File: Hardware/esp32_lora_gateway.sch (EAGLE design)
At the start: 36 parts, among them J5 U.FL, Q2 MBT3904DW1T1, U1 ESP-WROOM-32NARROW, U2 RFM96W, U3 3.3V, U5 CH340C

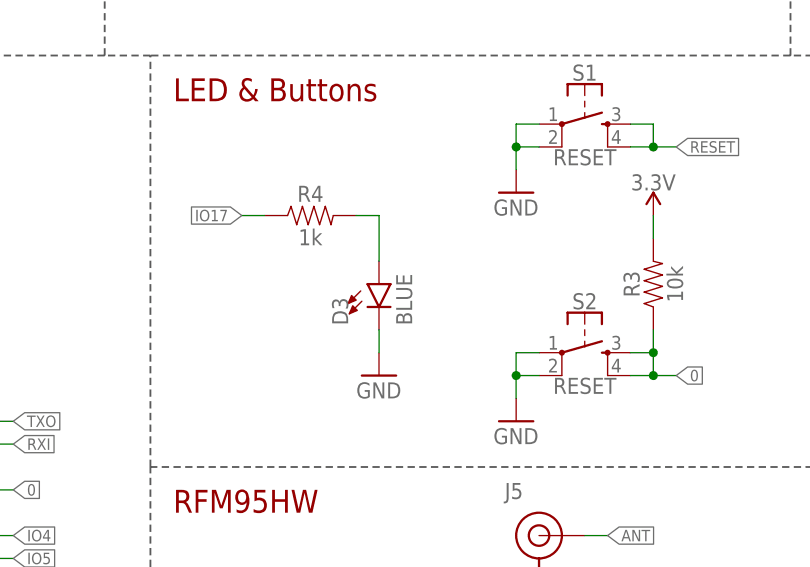
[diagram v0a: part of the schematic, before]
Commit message: Changing blue LED to green.
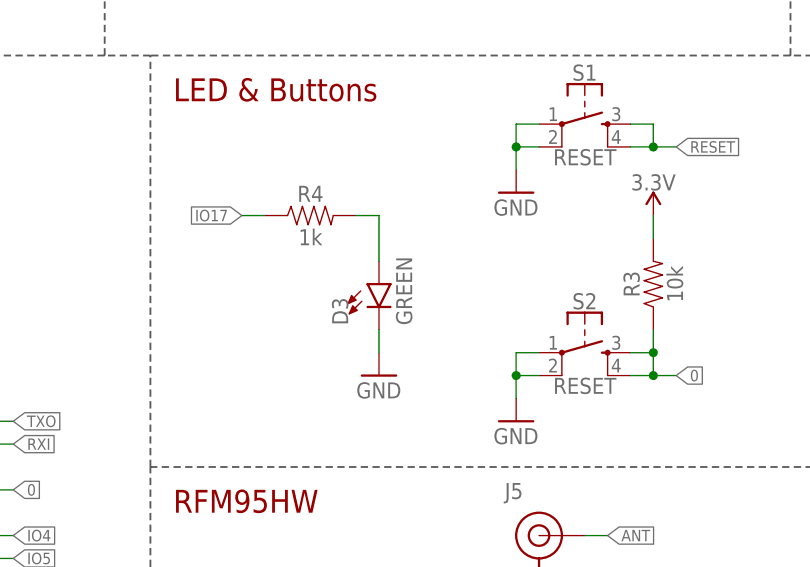
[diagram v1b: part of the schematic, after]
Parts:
- D3: value BLUE -> GREEN; device SparkFun-LED:LED-BLUE0603 -> SparkFun-LED:LED-GREEN0603
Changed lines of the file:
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@@
 <?xml version="1.0" encoding="utf-8"?>
 <!DOCTYPE eagle SYSTEM "eagle.dtd">
-<eagle version="9.0.1">
+<eagle version="9.1.1">
 <drawing>
 <settings>
@@
 <part name="S1" library="SparkFun-Switches" deviceset="MOMENTARY-SWITCH-SPST-2" device="-SMD-4.6X2.8MM" value="RESET"/>
 <part name="GND8" library="SparkFun-Aesthetics" deviceset="GND" device=""/>
-<part name="D3" library="SparkFun-LED" deviceset="LED-BLUE" device="0603" value="BLUE"/>
+<part name="D3" library="SparkFun-LED" deviceset="LED-GREEN" device="0603" value="GREEN"/>
 <part name="R4" library="SparkFun-Resistors" deviceset="1KOHM" device="-0603-1/10W-1%" value="1k"/>
 <part name="GND13" library="SparkFun-Aesthetics" deviceset="GND" device=""/>

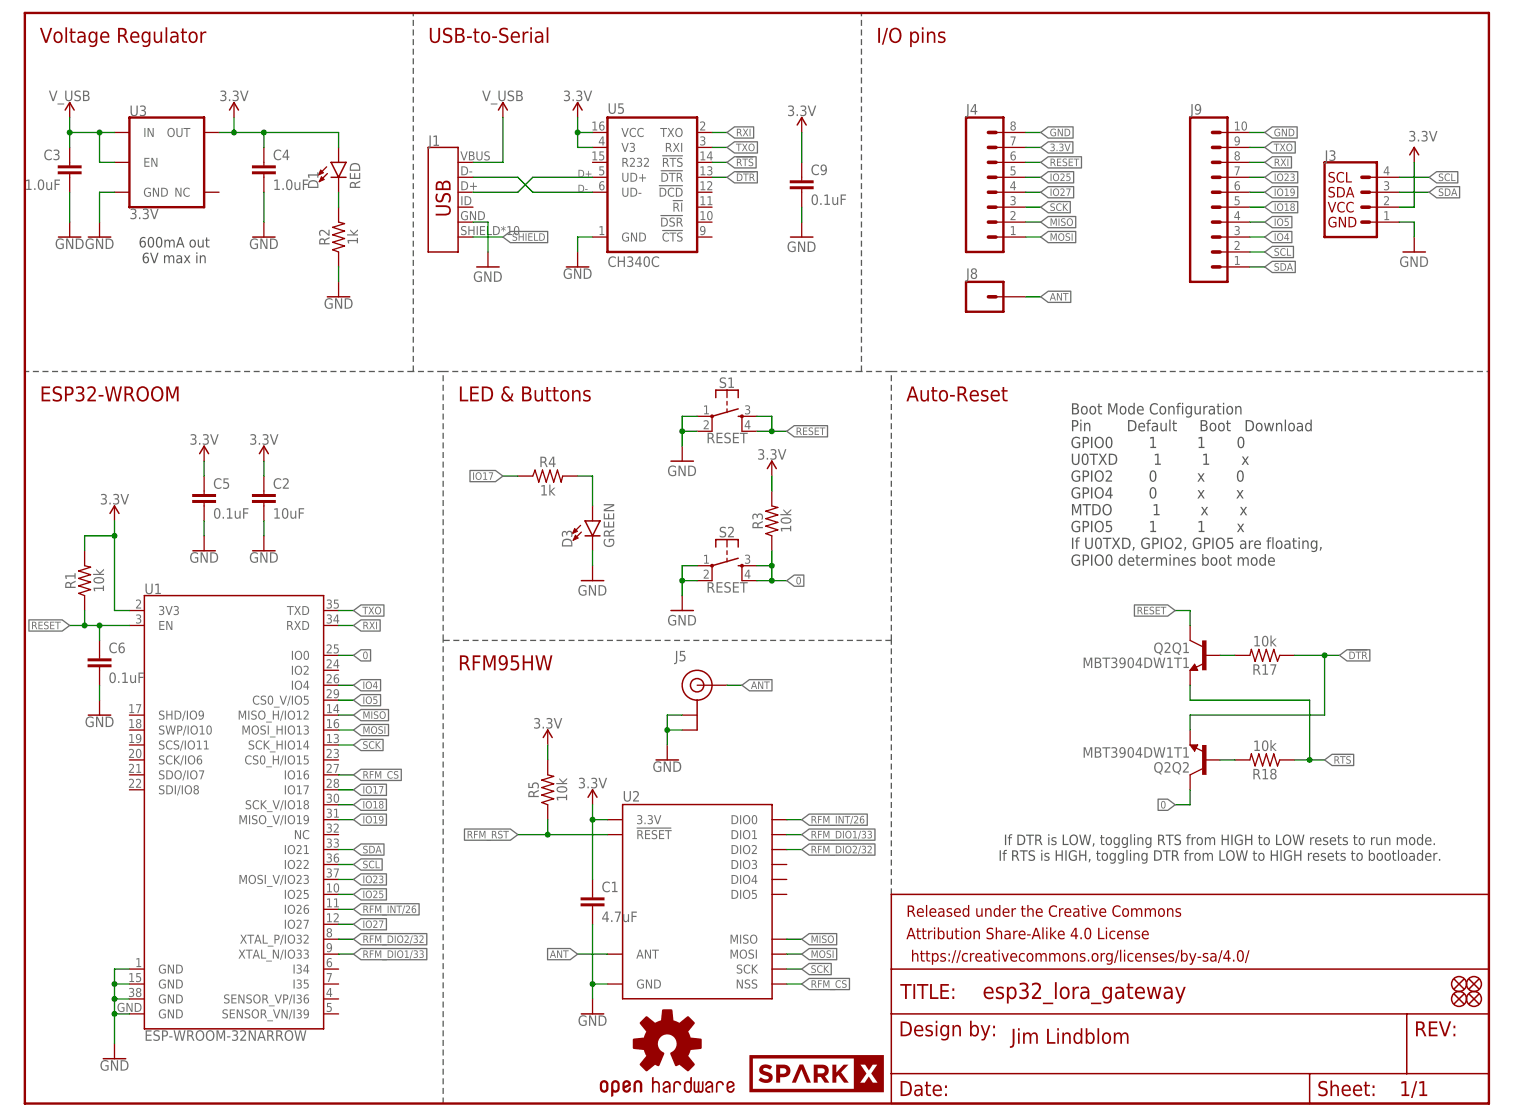
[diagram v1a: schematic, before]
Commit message: Moving part value text for assembly sheet. Set sch version.
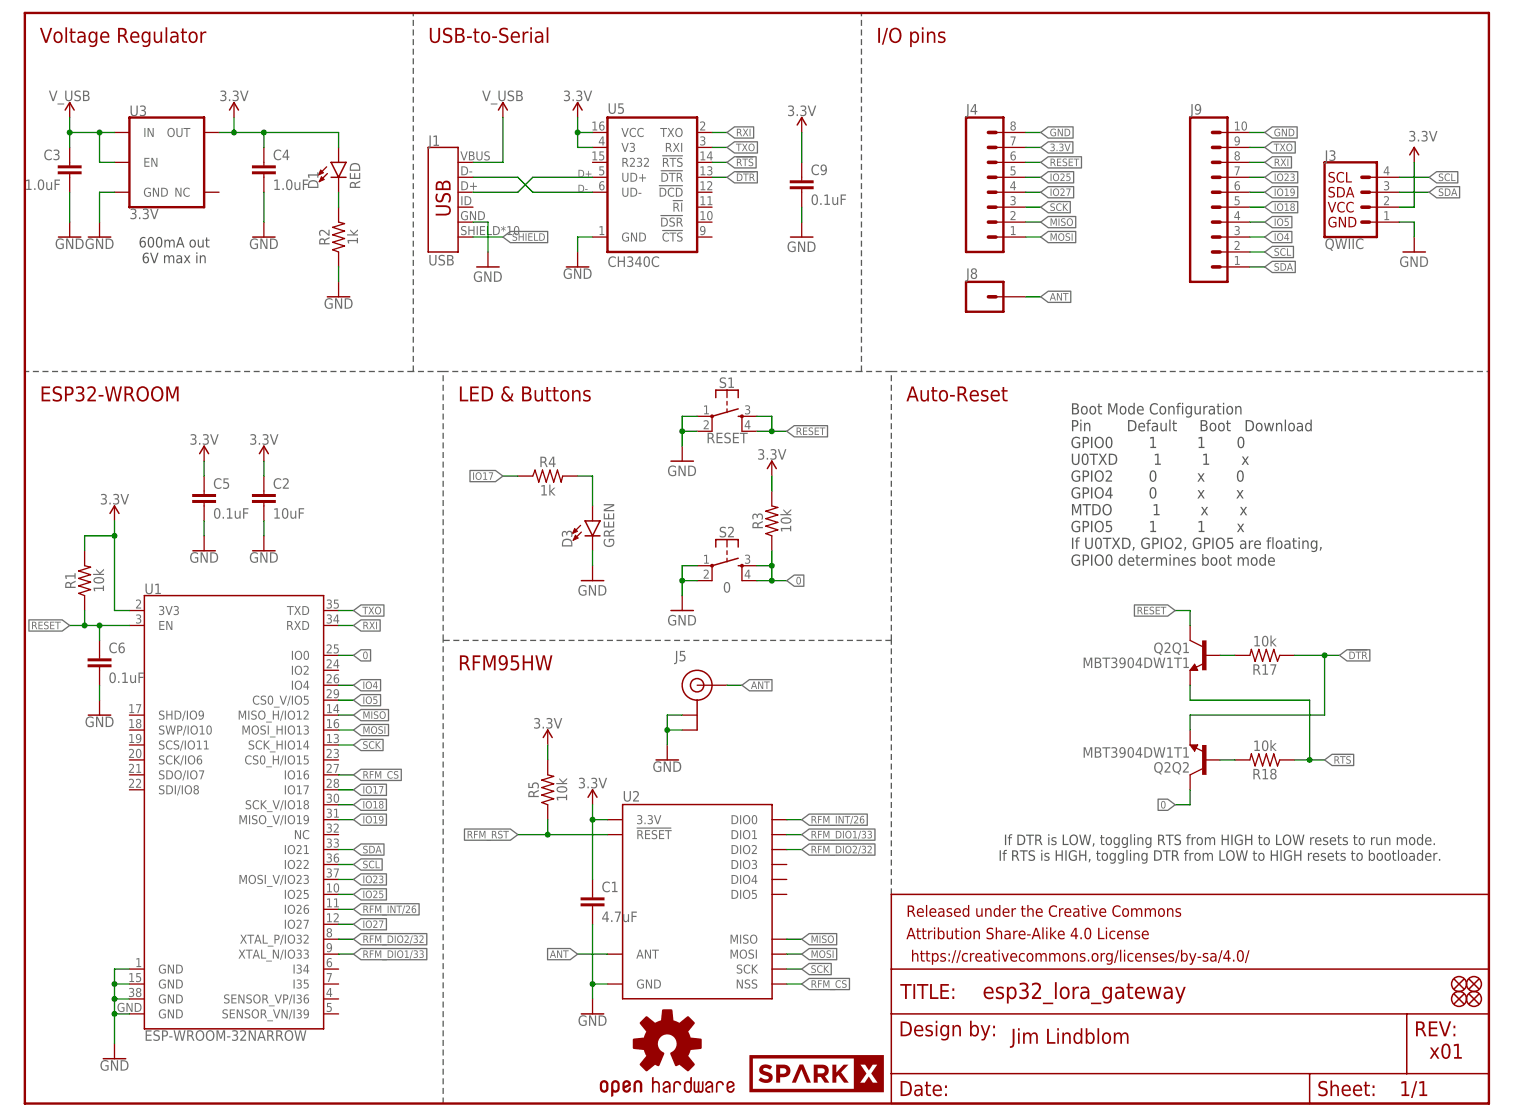
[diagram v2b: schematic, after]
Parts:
- J1: value (none) -> USB
- J3: value (none) -> QWIIC
- S2: value RESET -> 0
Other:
- note added: "x01"
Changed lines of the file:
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@@
 <part name="GND10" library="SparkFun-Aesthetics" deviceset="GND" device=""/>
 <part name="C9" library="SparkFun-Capacitors" deviceset="0.1UF-25V(+80/-20%)(0603)" device="" value="0.1uF"/>
-<part name="J1" library="SparkFun-Connectors" deviceset="USB_MICRO-B" device="_HALF_PTH_MILL"/>
+<part name="J1" library="SparkFun-Connectors" deviceset="USB_MICRO-B" device="_HALF_PTH_MILL" value="USB"/>
 <part name="SUPPLY4" library="SparkFun-PowerSymbols" deviceset="3.3V" device=""/>
 <part name="U3" library="SparkFun-IC-Power" deviceset="V_REG_AP2112" device="K-3.3V" value="3.3V"/>
@@
 <part name="GND4" library="SparkFun-PowerSymbols" deviceset="GND" device=""/>
 <part name="GND5" library="SparkFun-PowerSymbols" deviceset="GND" device=""/>
-<part name="J3" library="SparkFun-Connectors" deviceset="QWIIC_CONNECTOR" device="JS-1MM"/>
+<part name="J3" library="SparkFun-Connectors" deviceset="QWIIC_CONNECTOR" device="JS-1MM" value="QWIIC"/>
 <part name="SUPPLY7" library="SparkFun-Aesthetics" deviceset="3.3V" device=""/>
 <part name="GND7" library="SparkFun-Aesthetics" deviceset="GND" device=""/>
@@
 <part name="GND12" library="SparkFun-PowerSymbols" deviceset="GND" device=""/>
 <part name="SUPPLY9" library="SparkFun-PowerSymbols" deviceset="3.3V" device=""/>
-<part name="S2" library="SparkFun-Switches" deviceset="MOMENTARY-SWITCH-SPST-2" device="-SMD-4.6X2.8MM" value="RESET"/>
+<part name="S2" library="SparkFun-Switches" deviceset="MOMENTARY-SWITCH-SPST-2" device="-SMD-4.6X2.8MM" value="0"/>
 <part name="GND9" library="SparkFun-Aesthetics" deviceset="GND" device=""/>
 <part name="R2" library="SparkFun-Resistors" deviceset="1KOHM" device="-0603-1/10W-1%" value="1k"/>
@@
 <wire x1="66.04" y1="124.46" x2="66.04" y2="185.42" width="0.2032" layer="97" style="shortdash"/>
 <text x="167.64" y="10.16" size="2.54" layer="94">Jim Lindblom</text>
+<text x="238.76" y="7.62" size="2.54" layer="94">x01</text>
 </plain>
 <instances>
